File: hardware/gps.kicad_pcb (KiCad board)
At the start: 2 copper layers, 40 x 35 mm, 29 parts, among them P101 CON-SENSOR, P103 Boot, P104 U.FL, U101 XMC1XXX24, U102 FireFlyX1, U103 DRILL, U104 DRILL, U105 DRILL, U106 DRILL

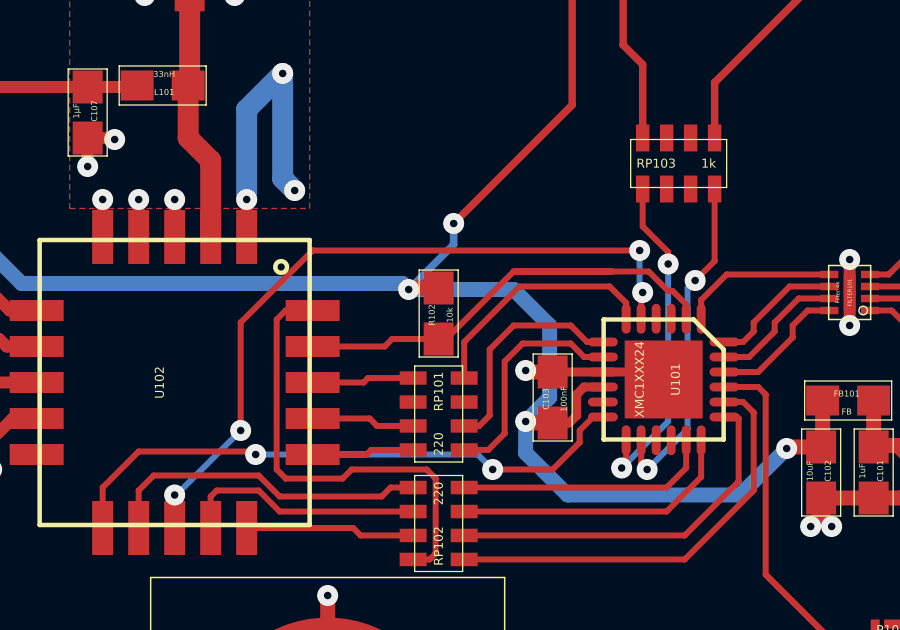
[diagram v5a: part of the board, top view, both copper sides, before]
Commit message: drc check, change reset pullup 10k->1k
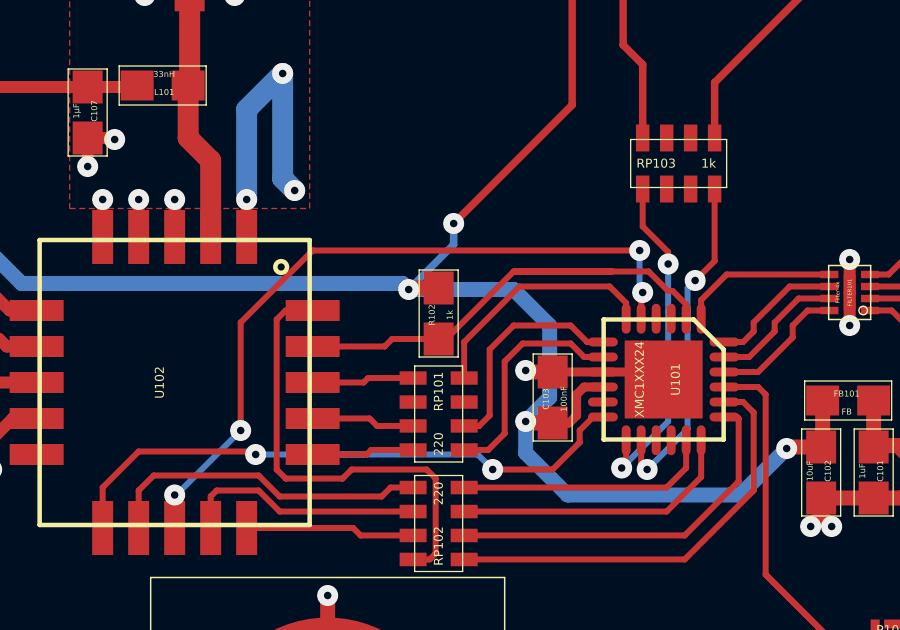
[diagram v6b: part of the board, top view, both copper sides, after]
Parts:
- added G***: LOGO, kicad-libraries:Logo_CoMCU, B.Cu at (186.4, 103.4)
- R102: value 10k -> 1k
- moved VAL 1.00 mm to (177.9, 103.4)
- moved VAL 1.00 mm to (194.9, 103.4)

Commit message: add fiducials
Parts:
- added Fiducial_Mark: VAL**, kicad-libraries:Fiducial_Mark, F.Cu at (204.9, 113.4)
- added Fiducial_Mark: VAL**, kicad-libraries:Fiducial_Mark, F.Cu at (167.9, 92.9)
- added Fiducial_Mark: VAL**, kicad-libraries:Fiducial_Mark, F.Cu at (199.9, 91.4)
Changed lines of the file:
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@@
     (tracks 348)
     (zones 0)
-    (modules 30)
+    (modules 33)
     (nets 36)
   )
   (page A4)
   (layers
-    (0 F.Cu signal hide)
+    (0 F.Cu signal)
     (31 B.Cu signal hide)
     (32 B.Adhes user)
@@
       (xy 1.301301 2.715081) (xy 1.302426 2.714986)) (layer B.SilkS) (width 0.01))
   )
+  (module kicad-libraries:Fiducial_Mark (layer F.Cu)
+    (at 204.9 113.4)
+    (attr smd)
+    (fp_text reference Fiducial_Mark (at 0 0) (layer F.SilkS) hide
+      (effects (font (size 0.127 0.127) (thickness 0.03302)))
+    )
+    (fp_text value VAL** (at 0 -0.29972) (layer F.SilkS) hide
+      (effects (font (size 0.127 0.127) (thickness 0.03302)))
+    )
+    (fp_circle (center 0 0) (end 1.15062 0) (layer Dwgs.User) (width 0.01016))
+    (pad 1 smd circle (at 0 0) (size 1.00076 1.00076) (layers F.Cu F.Paste F.Mask)
+      (clearance 0.65024))
+  )
+  (module kicad-libraries:Fiducial_Mark (layer F.Cu)
+    (at 167.9 92.9)
+    (attr smd)
+    (fp_text reference Fiducial_Mark (at 0 0) (layer F.SilkS) hide
+      (effects (font (size 0.127 0.127) (thickness 0.03302)))
+    )
+    (fp_text value VAL** (at 0 -0.29972) (layer F.SilkS) hide
+      (effects (font (size 0.127 0.127) (thickness 0.03302)))
+    )
+    (fp_circle (center 0 0) (end 1.15062 0) (layer Dwgs.User) (width 0.01016))
+    (pad 1 smd circle (at 0 0) (size 1.00076 1.00076) (layers F.Cu F.Paste F.Mask)
+      (clearance 0.65024))
+  )
+  (module kicad-libraries:Fiducial_Mark (layer F.Cu)
+    (at 199.9 91.4)
+    (attr smd)
+    (fp_text reference Fiducial_Mark (at 0 0) (layer F.SilkS) hide
+      (effects (font (size 0.127 0.127) (thickness 0.03302)))
+    )
+    (fp_text value VAL** (at 0 -0.29972) (layer F.SilkS) hide
+      (effects (font (size 0.127 0.127) (thickness 0.03302)))
+    )
+    (fp_circle (center 0 0) (end 1.15062 0) (layer Dwgs.User) (width 0.01016))
+    (pad 1 smd circle (at 0 0) (size 1.00076 1.00076) (layers F.Cu F.Paste F.Mask)
+      (clearance 0.65024))
+  )
   (gr_text Fix (at 190 89.3) (layer F.SilkS)

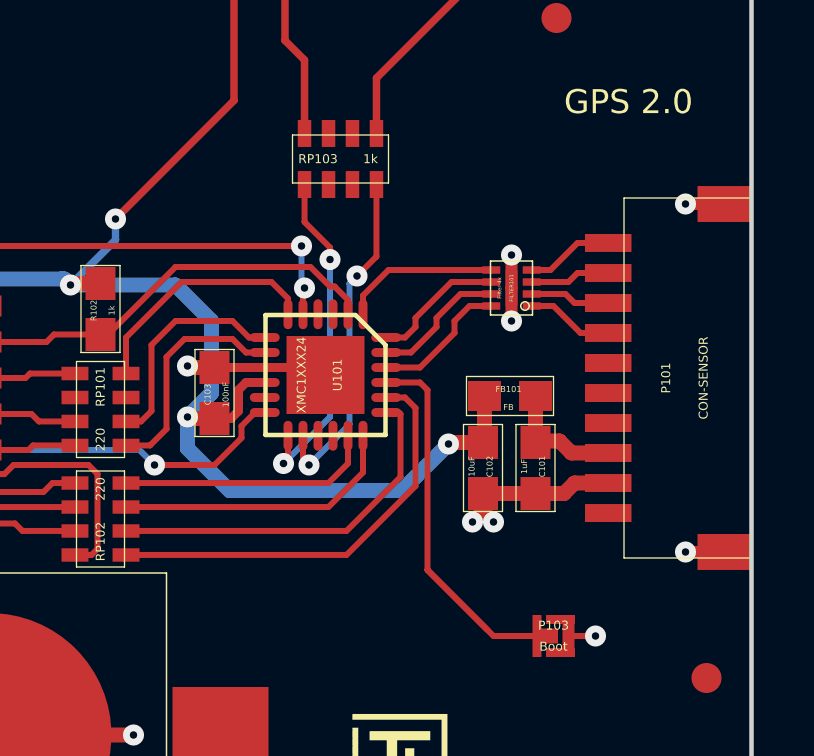
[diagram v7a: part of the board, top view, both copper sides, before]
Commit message: change bricklet connector to 7pole JST GH
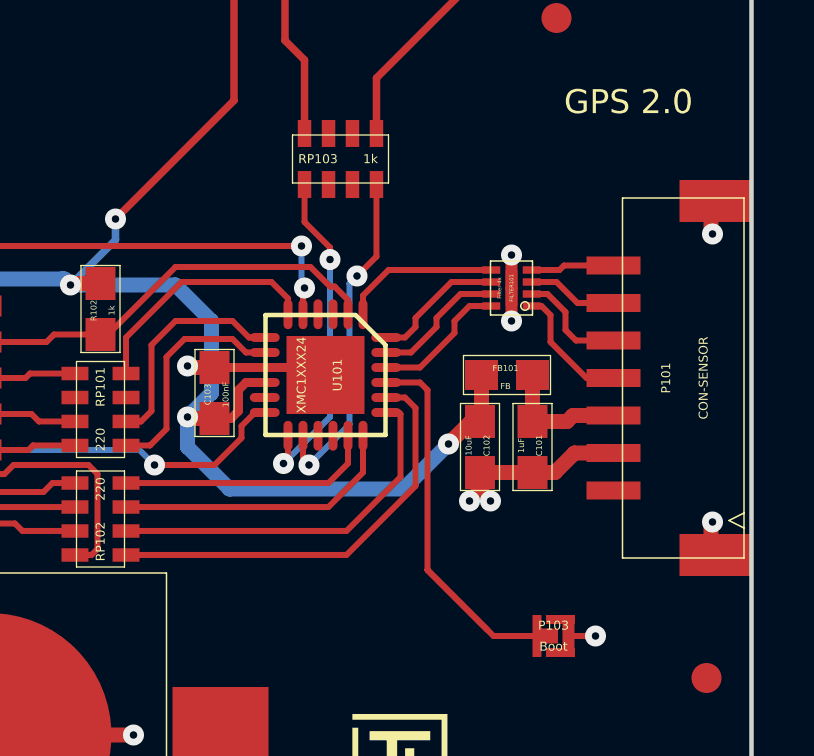
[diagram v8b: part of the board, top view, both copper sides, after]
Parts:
- P101: footprint kicad-libraries:CON-SENSOR -> kicad-libraries:CON-SENSOR2
- moved C101 0.71 mm to (199.1, 105.7)
- moved C102 0.71 mm to (197.3, 105.7)
- moved FB101 0.71 mm to (198.2, 103.3)
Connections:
- P101 pad 4: (no net) -> Net-(FILTER101-Pad1)
- P101 pad 5: (no net) -> Net-(FILTER101-Pad2)
- P101 pad 6: (no net) -> Net-(FILTER101-Pad3)
- P101 pad 7: Net-(FILTER101-Pad1) -> Net-(FILTER101-Pad4)
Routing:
- net Net-(FILTER101-Pad1): track 2.92 -> 4.25 mm
- net Net-(FILTER101-Pad2): track 2.67 -> 3.72 mm
